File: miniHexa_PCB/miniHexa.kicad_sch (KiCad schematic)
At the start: 16 parts, among them U1 STM32F401RETx, Y1 16Mhz

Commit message: update
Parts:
- removed C2: 20p, Capacitor_SMD:C_0805_2012Metric, symbol Device:C
- removed Y1: 16Mhz, Crystal:Crystal_HC49-4H_Vertical, symbol Device:Crystal
- added C26: 100nF, Capacitor_SMD:C_0805_2012Metric, symbol Device:C
- added Y2: 25mhz, Oscillator:Oscillator_SMD_Abracon_ASE-4Pin_3.2x2.5mm, symbol Oscillator:ASE-xxxMHz
- C1: value 20p -> 20uF; footprint Capacitor_SMD:C_0805_2012Metric -> (none)
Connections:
- net GND: now also C26.2, Y2.2 (GND)
- net at U1.30 (VCAP1): now also C1.2
- net at U1.5 (PH0): now also C26.1, Y2.3 (OUT); no longer C1.2
- new net: Y2.1 (EN), Y2.4 (Vdd)

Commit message: simple update
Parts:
- C1: footprint (none) -> Capacitor_SMD:C_0402_1005Metric
- C10: value 1u -> 1uF; footprint Capacitor_SMD:C_0805_2012Metric -> Capacitor_SMD:C_0402_1005Metric
- C13, C26, C3, C4, C5, C6, C7, C8, C9: footprint Capacitor_SMD:C_0805_2012Metric -> Capacitor_SMD:C_0402_1005Metric
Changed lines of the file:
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@@
 			)
 		)
-		(property "Footprint" "Capacitor_SMD:C_0805_2012Metric"
+		(property "Footprint" "Capacitor_SMD:C_0402_1005Metric"
 			(at 122.8852 27.94 0)
 			(hide yes)
@@
 			)
 		)
-		(property "Footprint" "Capacitor_SMD:C_0805_2012Metric"
+		(property "Footprint" "Capacitor_SMD:C_0402_1005Metric"
 			(at 44.1452 62.23 0)
 			(hide yes)
@@
 			)
 		)
-		(property "Footprint" "Capacitor_SMD:C_0805_2012Metric"
+		(property "Footprint" "Capacitor_SMD:C_0402_1005Metric"
 			(at 88.5952 27.94 0)
 			(hide yes)
@@
 			)
 		)
-		(property "Footprint" ""
+		(property "Footprint" "Capacitor_SMD:C_0402_1005Metric"
 			(at 82.55 109.5248 0)
 			(hide yes)
@@
 			)
 		)
-		(property "Footprint" "Capacitor_SMD:C_0805_2012Metric"
+		(property "Footprint" "Capacitor_SMD:C_0402_1005Metric"
 			(at 77.1652 27.94 0)
 			(hide yes)
@@
 			)
 		)
-		(property "Footprint" "Capacitor_SMD:C_0805_2012Metric"
+		(property "Footprint" "Capacitor_SMD:C_0402_1005Metric"
 			(at 40.3352 27.94 0)
 			(hide yes)
@@
 			)
 		)
-		(property "Footprint" "Capacitor_SMD:C_0805_2012Metric"
+		(property "Footprint" "Capacitor_SMD:C_0402_1005Metric"
 			(at 135.5852 27.94 0)
 			(hide yes)
@@
 			)
 		)
-		(property "Footprint" "Capacitor_SMD:C_0805_2012Metric"
+		(property "Footprint" "Capacitor_SMD:C_0402_1005Metric"
 			(at 53.0352 27.94 0)
 			(hide yes)
@@
 			)
 		)
-		(property "Value" "1u"
+		(property "Value" "1uF"
 			(at 160.02 25.3999 0)
 			(show_name no)
@@
 			)
 		)
-		(property "Footprint" "Capacitor_SMD:C_0805_2012Metric"
+		(property "Footprint" "Capacitor_SMD:C_0402_1005Metric"
 			(at 157.1752 27.94 0)
 			(hide yes)
@@
 			)
 		)
-		(property "Footprint" "Capacitor_SMD:C_0805_2012Metric"
+		(property "Footprint" "Capacitor_SMD:C_0402_1005Metric"
 			(at 65.7352 27.94 0)
 			(hide yes)
@@
 			)
 		)
-		(property "Footprint" "Capacitor_SMD:C_0805_2012Metric"
+		(property "Footprint" "Capacitor_SMD:C_0402_1005Metric"
 			(at 42.8752 46.99 0)
 			(hide yes)

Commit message: layout phase pcb
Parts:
- removed MK-L1: INMP441-L, Audio_Module:MIC_INMP441ACEZ-R7, symbol Microphone:INMP441ACEZ-R7
- removed MK-R1: INMP441-R, Audio_Module:MIC_INMP441ACEZ-R7, symbol Microphone:INMP441ACEZ-R7
- removed R29: 100k, Resistor_SMD:R_0805_2012Metric, symbol Device:R
- added C30, C31: 100nF, Capacitor_SMD:C_0402_1005Metric, symbol Device:C
- added MK1: ICS-R, Sensor_Audio:InvenSense_ICS-43434-6_3.5x2.65mm, symbol Sensor_Audio:ICS-43434
- added MK2: ICS - L, Sensor_Audio:InvenSense_ICS-43434-6_3.5x2.65mm, symbol Sensor_Audio:ICS-43434
- added R1: 10k, Resistor_SMD:R_0402_1005Metric, symbol Device:R
- added R32: 100k, Resistor_SMD:R_0402_1005Metric, symbol Device:R
- added SW1: SW_Push, Button_Switch_SMD:SW_SPST_B3U-1000P, symbol Switch:SW_Push
- C8: value 10n -> 10nF
- C9: value 1u -> 1uF
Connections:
- net +3.3V: now also C30.2, C31.2, MK1.2 (LR), MK1.5 (VDD), MK2.5 (VDD), R1.2
- net GND: now also C30.1, C31.1, MK1.3 (GND), MK2.2 (LR), MK2.3 (GND), R32.2
- net MIC_SCK: now also MK1.4 (SCK), MK2.4 (SCK)
- net MIC_SD: now also MK1.6 (SD), MK2.6 (SD), R32.1
- net MIC_WS: now also MK1.1 (WS), MK2.1 (WS)
- net at C13.1, U1.7 (NRST): now also SW1.2
- new net: R1.1, SW1.1
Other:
- moved on the sheet: C13

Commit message: layout done
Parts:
- added R2: 0, Resistor_SMD:R_0402_1005Metric, symbol Device:R
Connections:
- net I2C_SCK: now also R2.1, R2.2
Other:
- note added: "R for jumping a trace"
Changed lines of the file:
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@@
 	(generator_version "10.0")
 	(paper "A4")
+	(text "R for jumping a trace"
+		(exclude_from_sim no)
+		(at 141.732 94.234 0)
+		(effects
+			(font
+				(size 1.27 1.27)
+			)
+		)
+	)
 	(text_box "Stereo Mic\n"
 		(exclude_from_sim no)
@@
 	(wire
 		(pts
+			(xy 135.89 97.79) (xy 132.08 97.79)
+		)
+		(stroke
+			(width 0)
+			(type default)
+		)
+	)
+	(wire
+		(pts
 			(xy 83.82 177.8) (xy 91.44 177.8)
 		)
@@
 	(wire
 		(pts
+			(xy 124.46 97.79) (xy 120.65 97.79)
+		)
+		(stroke
+			(width 0)
+			(type default)
+		)
+	)
+	(wire
+		(pts
 			(xy 102.87 31.75) (xy 105.41 31.75)
 		)
@@
 		)
 	)
-	(global_label "I2C_SCK"
-		(shape input)
-		(at 120.65 97.79 0)
-		(fields_autoplaced yes)
+	(label "I2C_SCK"
+		(at 121.92 97.79 0)
 		(effects
 			(font
 				(size 1.27 1.27)
 			)
+			(justify left bottom)
+		)
+	)
+	(global_label "I2C_SCK"
+		(shape input)
+		(at 135.89 97.79 0)
+		(fields_autoplaced yes)
+		(effects
+			(font
+				(size 1.27 1.27)
+			)
 			(justify left)
 		)
 		(property "Intersheetrefs" "${INTERSHEET_REFS}"
-			(at 131.4366 97.79 0)
+			(at 146.6766 97.79 0)
 			(hide yes)
 			(show_name no)
@@
 					(unit 1)
 				)
+			)
+		)
+	)
+	(symbol
+		(lib_id "Device:R")
+		(at 128.27 97.79 90)
+		(unit 1)
+		(body_style 1)
+		(exclude_from_sim no)
+		(in_bom yes)
+		(on_board yes)
+		(in_pos_files yes)
+		(dnp no)
+		(fields_autoplaced yes)
+		(property "Reference" "R2"
+			(at 128.27 91.44 90)
+			(show_name no)
+			(do_not_autoplace no)
+			(effects
+				(font
+					(size 1.27 1.27)
+				)
+			)
+		)
+		(property "Value" "0"
+			(at 128.27 93.98 90)
+			(show_name no)
+			(do_not_autoplace no)
+			(effects
+				(font
+					(size 1.27 1.27)
+				)
+			)
+		)
+		(property "Footprint" "Resistor_SMD:R_0402_1005Metric"
+			(at 128.27 99.568 90)
+			(hide yes)
+			(show_name no)
+			(do_not_autoplace no)
+			(effects
+				(font
+					(size 1.27 1.27)
+				)
+			)
+		)
+		(property "Datasheet" ""
+			(at 128.27 97.79 0)
+			(hide yes)
+			(show_name no)
+			(do_not_autoplace no)
+			(effects
+				(font
+					(size 1.27 1.27)
+				)
+			)
+		)
+		(property "Description" "Resistor"
+			(at 128.27 97.79 0)
+			(hide yes)
+			(show_name no)
+			(do_not_autoplace no)
+			(effects
+				(font
+					(size 1.27 1.27)
+				)
+			)
+		)
+		(pin "2"
+		)
+		(pin "1"
+		)
+		(instances
+			(project "miniHexa"
+				(path "/3449ee66-2977-4802-a474-0821cdf4e79b"
+					(reference "R2")
+					(unit 1)
+				)

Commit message: before auto routing
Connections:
- net +3.3V: now also Y2.1 (EN), Y2.4 (Vdd)
- no-connect marks 0 -> 1
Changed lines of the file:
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@@
+	)
+	(junction
+		(at 29.21 43.18)
+		(diameter 0)
+		(color 0 0 0 0)
 	)
 	(junction
@@
 		(diameter 0)
 		(color 0 0 0 0)
+	)
+	(no_connect
+		(at 85.09 57.15)
 	)
 	(wire
@@
 					(unit 1)
 				)
+			)
+		)
+	)
+	(symbol
+		(lib_id "power:+3.3V")
+		(at 29.21 43.18 0)
+		(unit 1)
+		(body_style 1)
+		(exclude_from_sim no)
+		(in_bom yes)
+		(on_board yes)
+		(in_pos_files yes)
+		(dnp no)
+		(fields_autoplaced yes)
+		(property "Reference" "#PWR014"
+			(at 29.21 46.99 0)
+			(hide yes)
+			(show_name no)
+			(do_not_autoplace no)
+			(effects
+				(font
+					(size 1.27 1.27)
+				)
+			)
+		)
+		(property "Value" "+3.3V"
+			(at 29.21 38.1 0)
+			(show_name no)
+			(do_not_autoplace no)
+			(effects
+				(font
+					(size 1.27 1.27)
+				)
+			)
+		)
+		(property "Footprint" ""
+			(at 29.21 43.18 0)
+			(hide yes)
+			(show_name no)
+			(do_not_autoplace no)
+			(effects
+				(font
+					(size 1.27 1.27)
+				)
+			)
+		)
+		(property "Datasheet" ""
+			(at 29.21 43.18 0)
+			(hide yes)
+			(show_name no)
+			(do_not_autoplace no)
+			(effects
+				(font
+					(size 1.27 1.27)
+				)
+			)
+		)
+		(property "Description" "Power symbol creates a global label with name \"+3.3V\""
+			(at 29.21 43.18 0)
+			(hide yes)
+			(show_name no)
+			(do_not_autoplace no)
+			(effects
+				(font
+					(size 1.27 1.27)
+				)
+			)
+		)
+		(pin "1"
+		)
+		(instances
+			(project "miniHexa"
+				(path "/3449ee66-2977-4802-a474-0821cdf4e79b"
+					(reference "#PWR014")
+					(unit 1)
+				)

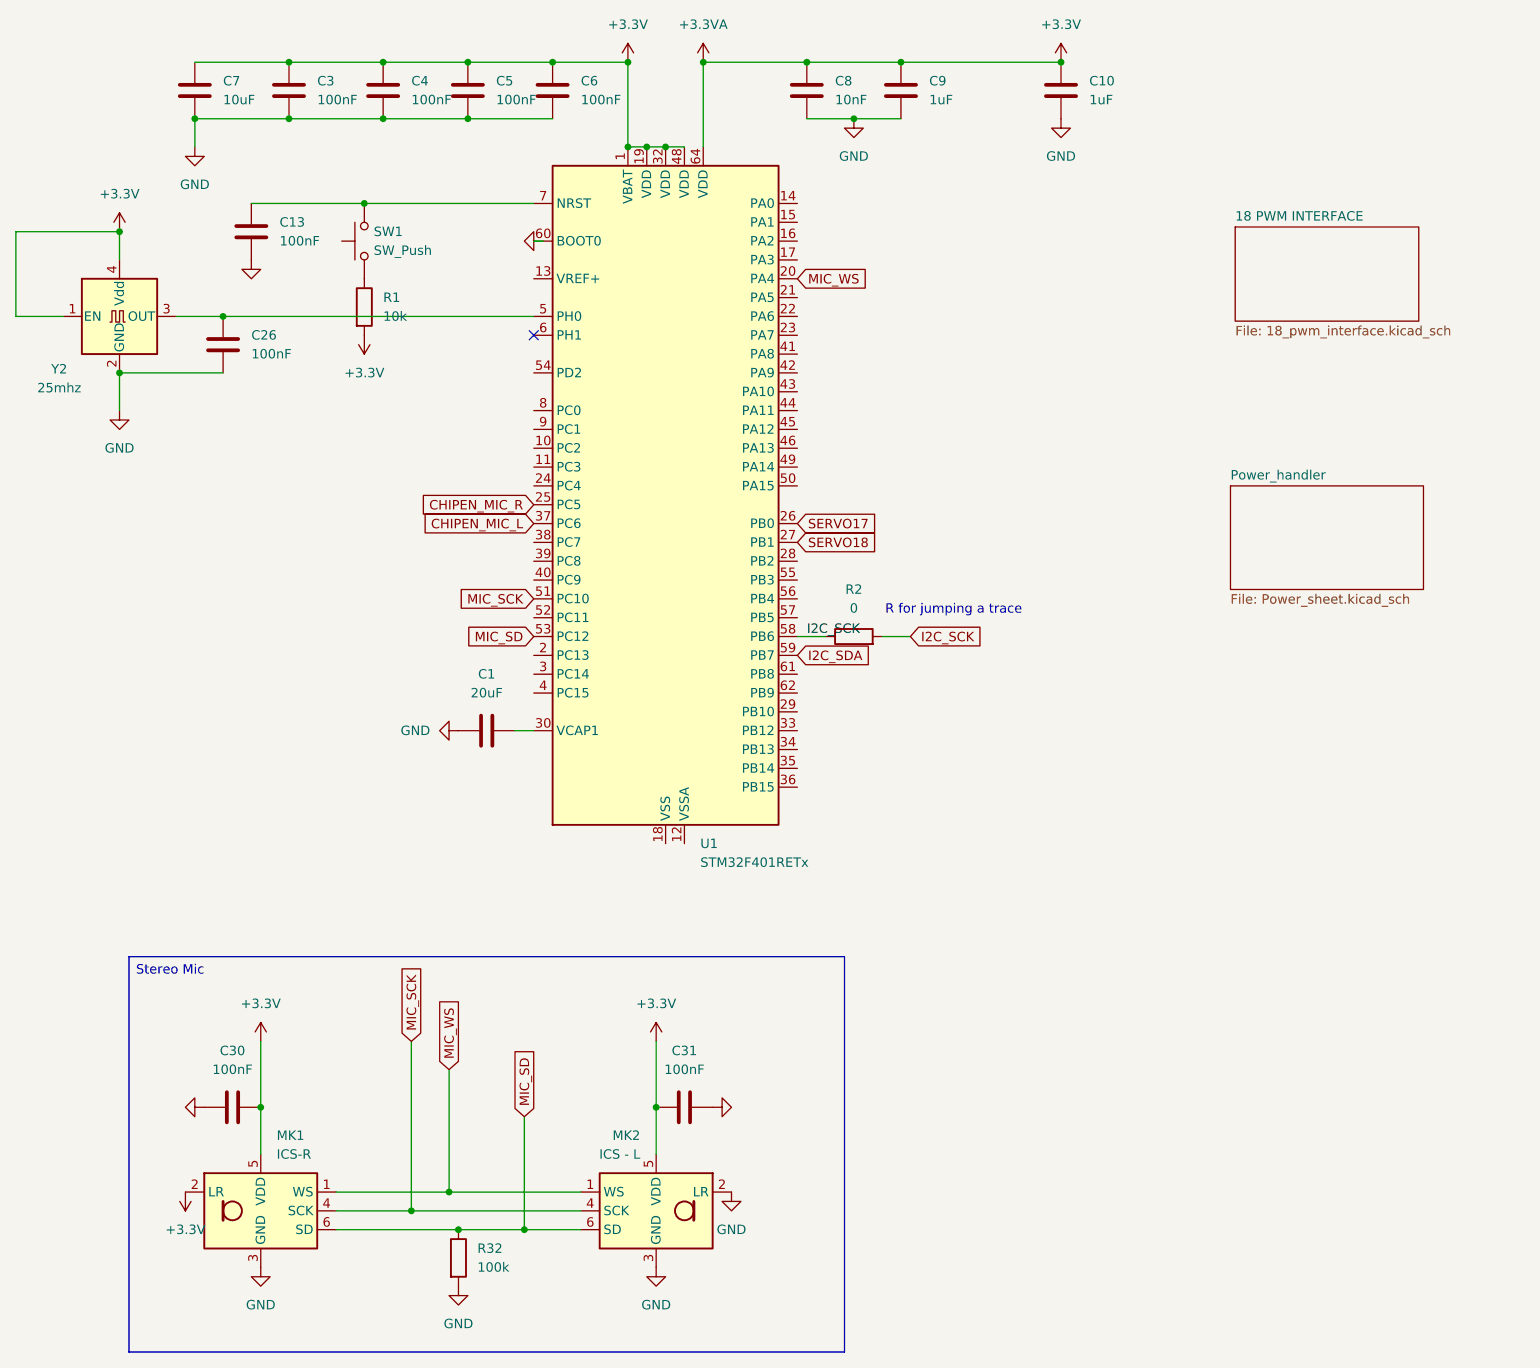
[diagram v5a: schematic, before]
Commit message: Decided to manually route, looks good
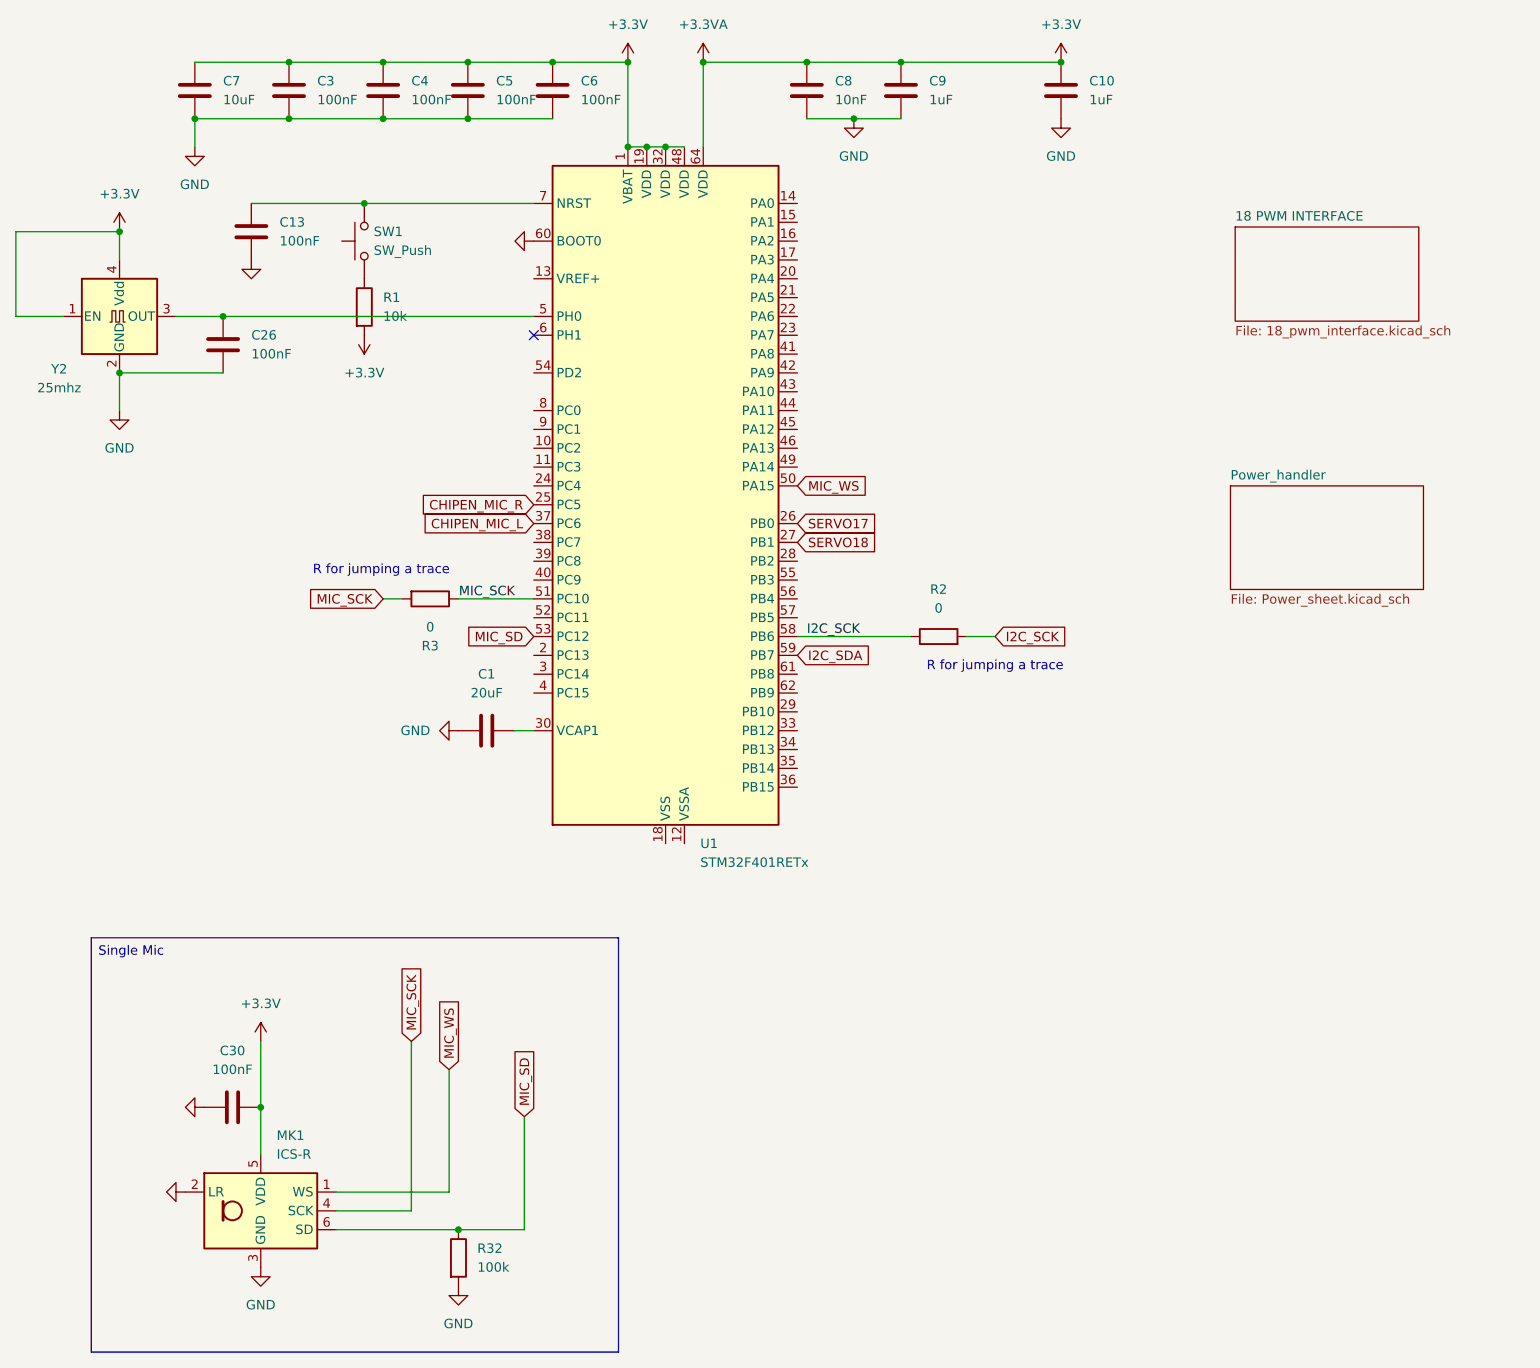
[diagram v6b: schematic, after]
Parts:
- removed C31: 100nF, Capacitor_SMD:C_0402_1005Metric, symbol Device:C
- removed MK2: ICS - L, Sensor_Audio:InvenSense_ICS-43434-6_3.5x2.65mm, symbol Sensor_Audio:ICS-43434
- added R3: 0, Resistor_SMD:R_0402_1005Metric, symbol Device:R
- C30: footprint Capacitor_SMD:C_0402_1005Metric -> Capacitor_SMD:C_0805_2012Metric
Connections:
- net +3.3V: no longer MK1.2 (LR)
- net GND: now also MK1.2 (LR)
- net MIC_SCK: now also R3.1, R3.2
- net MIC_WS: now also U1.50 (PA15); no longer U1.20 (PA4)
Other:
- moved on the sheet: R2

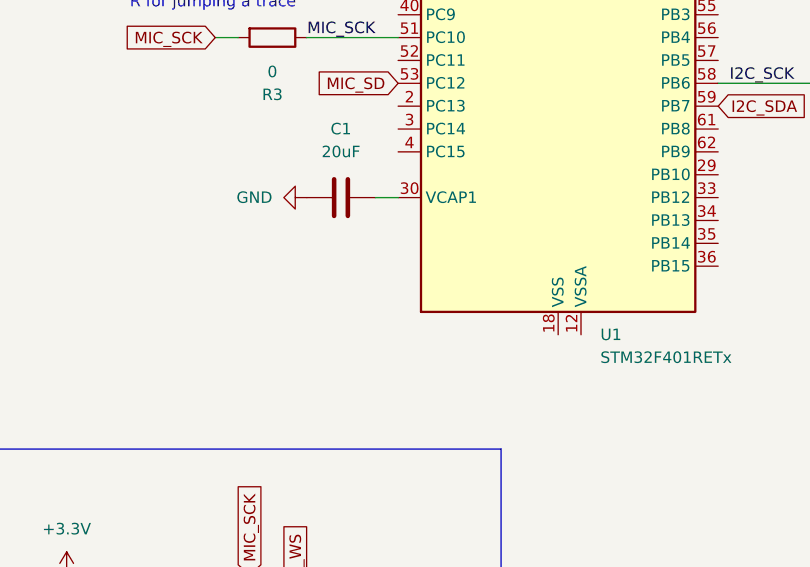
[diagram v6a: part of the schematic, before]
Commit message: routing complete with drc
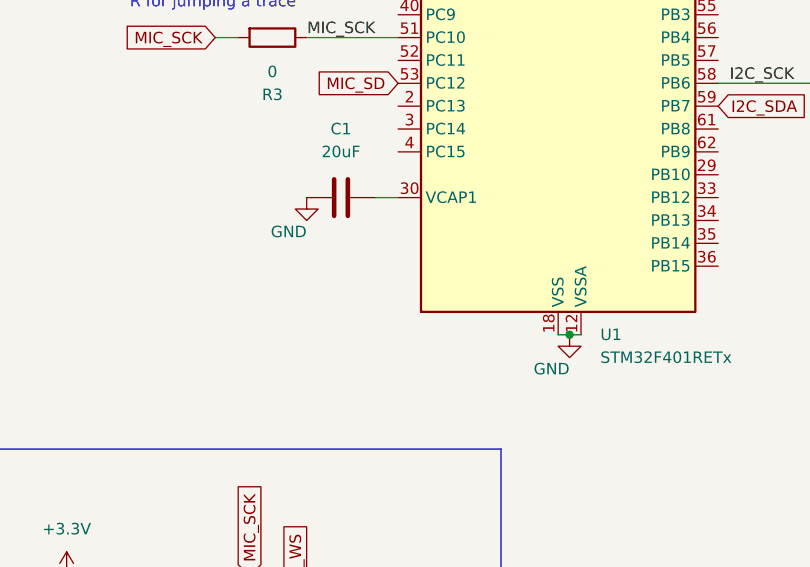
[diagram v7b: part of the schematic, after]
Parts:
- R2, R3: footprint Resistor_SMD:R_0402_1005Metric -> Resistor_SMD:R_0603_1608Metric
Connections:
- net GND: now also U1.12 (VSSA), U1.18 (VSS), U1.31 (VSS), U1.47 (VSS), U1.63 (VSS)
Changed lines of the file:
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@@
+	)
+	(junction
+		(at 104.14 125.73)
+		(diameter 0)
+		(color 0 0 0 0)
 	)
 	(junction
@@
 	(wire
 		(pts
+			(xy 104.14 125.73) (xy 105.41 125.73)
+		)
+		(stroke
+			(width 0)
+			(type default)
+		)
+	)
+	(wire
+		(pts
 			(xy 58.42 177.8) (xy 74.93 177.8)
+		)
+		(stroke
+			(width 0)
+			(type default)
+		)
+	)
+	(wire
+		(pts
+			(xy 102.87 125.73) (xy 104.14 125.73)
 		)
 		(stroke
@@
 	(symbol
 		(lib_id "power:GND")
+		(at 104.14 125.73 0)
+		(unit 1)
+		(body_style 1)
+		(exclude_from_sim no)
+		(in_bom yes)
+		(on_board yes)
+		(in_pos_files yes)
+		(dnp no)
+		(property "Reference" "#PWR033"
+			(at 104.14 132.08 0)
+			(hide yes)
+			(show_name no)
+			(do_not_autoplace no)
+			(effects
+				(font
+					(size 1.27 1.27)
+				)
+			)
+		)
+		(property "Value" "GND"
+			(at 104.1399 129.54 0)
+			(show_name no)
+			(do_not_autoplace no)
+			(effects
+				(font
+					(size 1.27 1.27)
+				)
+				(justify right)
+			)
+		)
+		(property "Footprint" ""
+			(at 104.14 125.73 0)
+			(hide yes)
+			(show_name no)
+			(do_not_autoplace no)
+			(effects
+				(font
+					(size 1.27 1.27)
+				)
+			)
+		)
+		(property "Datasheet" ""
+			(at 104.14 125.73 0)
+			(hide yes)
+			(show_name no)
+			(do_not_autoplace no)
+			(effects
+				(font
+					(size 1.27 1.27)
+				)
+			)
+		)
+		(property "Description" "Power symbol creates a global label with name \"GND\" , ground"
+			(at 104.14 125.73 0)
+			(hide yes)
+			(show_name no)
+			(do_not_autoplace no)
+			(effects
+				(font
+					(size 1.27 1.27)
+				)
+			)
+		)
+		(pin "1"
+		)
+		(instances
+			(project "miniHexa"
+				(path "/3449ee66-2977-4802-a474-0821cdf4e79b"
+					(reference "#PWR033")
+					(unit 1)
+				)
+			)
+		)
+	)
+	(symbol
+		(lib_id "power:GND")
 		(at 128.27 27.94 0)
 		(unit 1)
@@
 	(symbol
 		(lib_id "power:GND")
-		(at 74.93 110.49 270)
+		(at 74.93 110.49 0)
 		(unit 1)
 		(body_style 1)
@@
 		(in_pos_files yes)
 		(dnp no)
-		(fields_autoplaced yes)
 		(property "Reference" "#PWR011"
-			(at 68.58 110.49 0)
+			(at 74.93 116.84 0)
 			(hide yes)
 			(show_name no)
@@
 		)
 		(property "Value" "GND"
-			(at 71.12 110.4899 90)
+			(at 74.9299 114.3 0)
 			(show_name no)
 			(do_not_autoplace no)
@@
 			)
 		)
-		(property "Footprint" "Resistor_SMD:R_0402_1005Metric"
+		(property "Footprint" "Resistor_SMD:R_0603_1608Metric"
 			(at 71.12 90.932 90)
 			(hide yes)
@@
 			)
 		)
-		(property "Footprint" "Resistor_SMD:R_0402_1005Metric"
+		(property "Footprint" "Resistor_SMD:R_0603_1608Metric"
 			(at 139.7 99.568 90)
 			(hide yes)
